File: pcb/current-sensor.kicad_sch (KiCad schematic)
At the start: 34 parts, among them U1 SS39ET, U2 TLV9064, U3 SS39ET

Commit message: Updated parts for cost
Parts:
- C1, C10, C4, C5: LCSC C106249 -> C21120; MN Yageo -> Samsung; MPN CC0603KRX7R7BB224 -> CL10B224KA8NNNC
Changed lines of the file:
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@@
 			)
 		)
-		(property "Description" "16V 220nF X7R ±10% 0603 Multilayer Ceramic Capacitors MLCC"
+		(property "Description" "25V 220nF X7R ±10% 0603 Multilayer Ceramic Capacitors MLCC"
 			(at 162.56 71.12 0)
 			(effects
@@
 			)
 		)
-		(property "MN" "Yageo"
+		(property "MN" "Samsung"
 			(at 162.56 71.12 0)
 			(effects
@@
 			)
 		)
-		(property "MPN" "CC0603KRX7R7BB224"
+		(property "MPN" "CL10B224KA8NNNC"
 			(at 162.56 71.12 0)
 			(effects
@@
 			)
 		)
-		(property "LCSC" "C106249"
+		(property "LCSC" "C21120"
 			(at 162.56 71.12 0)
 			(effects
@@
 			)
 		)
-		(property "Description" "16V 220nF X7R ±10% 0603 Multilayer Ceramic Capacitors MLCC"
+		(property "Description" "25V 220nF X7R ±10% 0603 Multilayer Ceramic Capacitors MLCC"
 			(at 194.31 77.47 0)
 			(effects
@@
 			)
 		)
-		(property "MN" "Yageo"
+		(property "MN" "Samsung"
 			(at 194.31 77.47 0)
 			(effects
@@
 			)
 		)
-		(property "MPN" "CC0603KRX7R7BB224"
+		(property "MPN" "CL10B224KA8NNNC"
 			(at 194.31 77.47 0)
 			(effects
@@
 			)
 		)
-		(property "LCSC" "C106249"
+		(property "LCSC" "C21120"
 			(at 194.31 77.47 0)
 			(effects
@@
 			)
 		)
-		(property "Description" "16V 220nF X7R ±10% 0603 Multilayer Ceramic Capacitors MLCC"
+		(property "Description" "25V 220nF X7R ±10% 0603 Multilayer Ceramic Capacitors MLCC"
 			(at 146.05 154.94 0)
 			(effects
@@
 			)
 		)
-		(property "MN" "Yageo"
+		(property "MN" "Samsung"
 			(at 146.05 154.94 0)
 			(effects
@@
 			)
 		)
-		(property "MPN" "CC0603KRX7R7BB224"
+		(property "MPN" "CL10B224KA8NNNC"
 			(at 146.05 154.94 0)
 			(effects
@@
 			)
 		)
-		(property "LCSC" "C106249"
+		(property "LCSC" "C21120"
 			(at 146.05 154.94 0)
 			(effects
@@
 			)
 		)
-		(property "Description" "16V 220nF X7R ±10% 0603 Multilayer Ceramic Capacitors MLCC"
+		(property "Description" "25V 220nF X7R ±10% 0603 Multilayer Ceramic Capacitors MLCC"
 			(at 208.28 41.91 0)
 			(effects
@@
 			)
 		)
-		(property "MN" "Yageo"
+		(property "MN" "Samsung"
 			(at 208.28 41.91 0)
 			(effects
@@
 			)
 		)
-		(property "MPN" "CC0603KRX7R7BB224"
+		(property "MPN" "CL10B224KA8NNNC"
 			(at 208.28 41.91 0)
 			(effects
@@
 			)
 		)
-		(property "LCSC" "C106249"
+		(property "LCSC" "C21120"
 			(at 208.28 41.91 0)
 			(effects

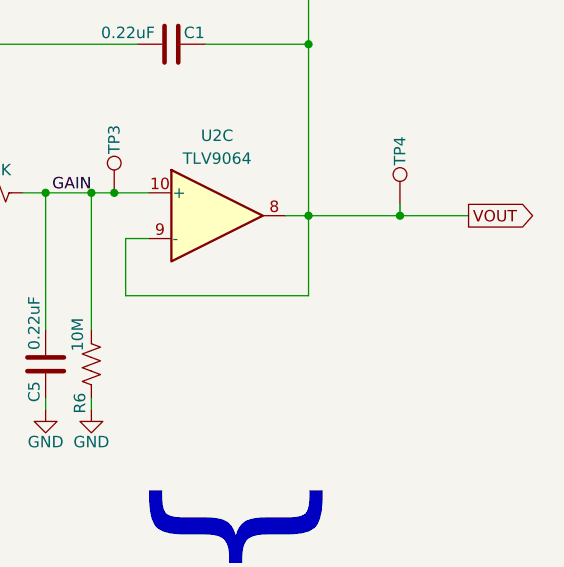
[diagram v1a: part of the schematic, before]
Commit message: Added TVS to ADC for spikes; still investigating
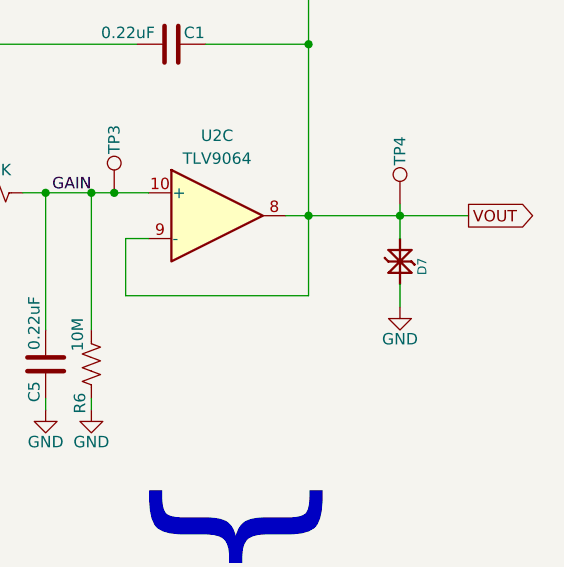
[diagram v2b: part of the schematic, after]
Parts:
- added D7: PESD3V3S1BL, CRGM Passive:DFN1006-2, symbol CRGM Passive:PESD3V3S1BL
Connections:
- net GND: now also D7.1 (K1)
- net VOUT: now also D7.2 (K2)
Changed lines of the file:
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@@
 	(wire
 		(pts
+			(xy 233.68 60.96) (xy 233.68 63.5)
+		)
+		(stroke
+			(width 0)
+			(type default)
+		)
+	)
+	(wire
+		(pts
 			(xy 123.19 74.93) (xy 123.19 55.88)
 		)
@@
 	(wire
 		(pts
+			(xy 233.68 68.58) (xy 233.68 71.12)
+		)
+		(stroke
+			(width 0)
+			(type default)
+		)
+	)
+	(wire
+		(pts
 			(xy 45.72 166.37) (xy 68.58 166.37)
 		)
@@
 	(symbol
 		(lib_id "power:GND")
+		(at 233.68 71.12 0)
+		(unit 1)
+		(exclude_from_sim no)
+		(in_bom yes)
+		(on_board yes)
+		(dnp no)
+		(property "Reference" "#PWR031"
+			(at 233.68 77.47 0)
+			(effects
+				(font
+					(size 1.27 1.27)
+				)
+				(hide yes)
+			)
+		)
+		(property "Value" "GND"
+			(at 233.68 74.676 0)
+			(effects
+				(font
+					(size 1.27 1.27)
+				)
+			)
+		)
+		(property "Footprint" ""
+			(at 233.68 71.12 0)
+			(effects
+				(font
+					(size 1.27 1.27)
+				)
+				(hide yes)
+			)
+		)
+		(property "Datasheet" ""
+			(at 233.68 71.12 0)
+			(effects
+				(font
+					(size 1.27 1.27)
+				)
+				(hide yes)
+			)
+		)
+		(property "Description" "Power symbol creates a global label with name \"GND\" , ground"
+			(at 233.68 71.12 0)
+			(effects
+				(font
+					(size 1.27 1.27)
+				)
+				(hide yes)
+			)
+		)
+		(pin "1"
+		)
+		(instances
+			(project "current-module"
+				(path "/a8149920-3b7f-4d7d-8e96-7a0b38870225/750b9b07-db7a-4289-8a61-542df9f7ebc0"
+					(reference "#PWR031")
+					(unit 1)
+				)
+			)
+		)
+	)
+	(symbol
+		(lib_id "power:GND")
 		(at 107.95 158.75 0)
 		(unit 1)
@@
 					(unit 1)
 				)
+			)
+		)
+	)
+	(symbol
+		(lib_id "CRGM Passive:PESD3V3S1BL")
+		(at 233.68 66.04 90)
+		(unit 1)
+		(exclude_from_sim no)
+		(in_bom yes)
+		(on_board yes)
+		(dnp no)
+		(property "Reference" "D7"
+			(at 236.728 67.564 0)
+			(effects
+				(font
+					(size 1 1)
+					(thickness 0.125)
+				)
+				(justify left bottom)
+			)
+		)
+		(property "Value" "PESD3V3S1BL"
+			(at 237.236 71.12 0)
+			(effects
+				(font
+					(size 1 1)
+					(thickness 0.125)
+				)
+				(justify left bottom)
+				(hide yes)
+			)
+		)
+		(property "Footprint" "CRGM Passive:DFN1006-2"
+			(at 238.76 65.786 0)
+			(effects
+				(font
+					(size 1.27 1.27)
+				)
+				(hide yes)
+			)
+		)
+		(property "Datasheet" "https://www.nexperia.com/product/PESD3V3S1BL"
+			(at 243.332 66.294 0)
+			(effects
+				(font
+					(size 1.27 1.27)
+				)
+				(hide yes)
+			)
+		)
+		(property "Description" "PESD3V3S1BL - Low capacitance bidirectional ESD protection diode\nVrwm=3.3v\nSource: https://assets.nexperia.com/documents/data-sheet/PESD3V3S1BL.pdf  Datasheet\nJLCPCB - C552521  Alternate https://jlcpcb.com/partdetail/DiodesIncorporated-DESD3V3S1BL7B/C500765 DESD3V3S1BL\nJLCPCB - C500765\nhttps://jlcpcb.com/partdetail/Fuxinsemi-LESD8D33CAT5G/C5563754 LESD8D3.3CAT5G\nJLCPCB - C5563754"
+			(at 252.73 64.516 0)
+			(effects
+				(font
+					(size 1.27 1.27)
+				)
+				(hide yes)
+			)
+		)
+		(property "LCSC" "C5563754"
+			(at 270.256 66.294 0)
+			(effects
+				(font
+					(size 1.27 1.27)
+				)
+				(hide yes)
+			)
+		)
+		(property "Digikey" "1727-PESD3V3S1BLYLTR-ND"
+			(at 268.224 65.278 0)
+			(effects
+				(font
+					(size 1.27 1.27)
+				)
+				(hide yes)
+			)
+		)
+		(property "Mouser" "621-DESD3V3S1BL-7B"
+			(at 266.192 64.516 0)
+			(effects
+				(font
+					(size 1.27 1.27)
+				)
+				(hide yes)
+			)
+		)
+		(property "MN" "FUXINSEMI"
+			(at 233.68 66.04 0)
+			(effects
+				(font
+					(size 1.27 1.27)
+				)
+				(hide yes)
+			)
+		)
+		(property "MPN" "LESD8D3.3CAT5G"
+			(at 233.68 66.04 0)
+			(effects
+				(font
+					(size 1.27 1.27)
+				)
+				(hide yes)
+			)
+		)
+		(pin "1"
+		)
+		(pin "2"
+		)
+		(instances
+			(project "current-module"
+				(path "/a8149920-3b7f-4d7d-8e96-7a0b38870225/750b9b07-db7a-4289-8a61-542df9f7ebc0"
+					(reference "D7")
+					(unit 1)
+				)

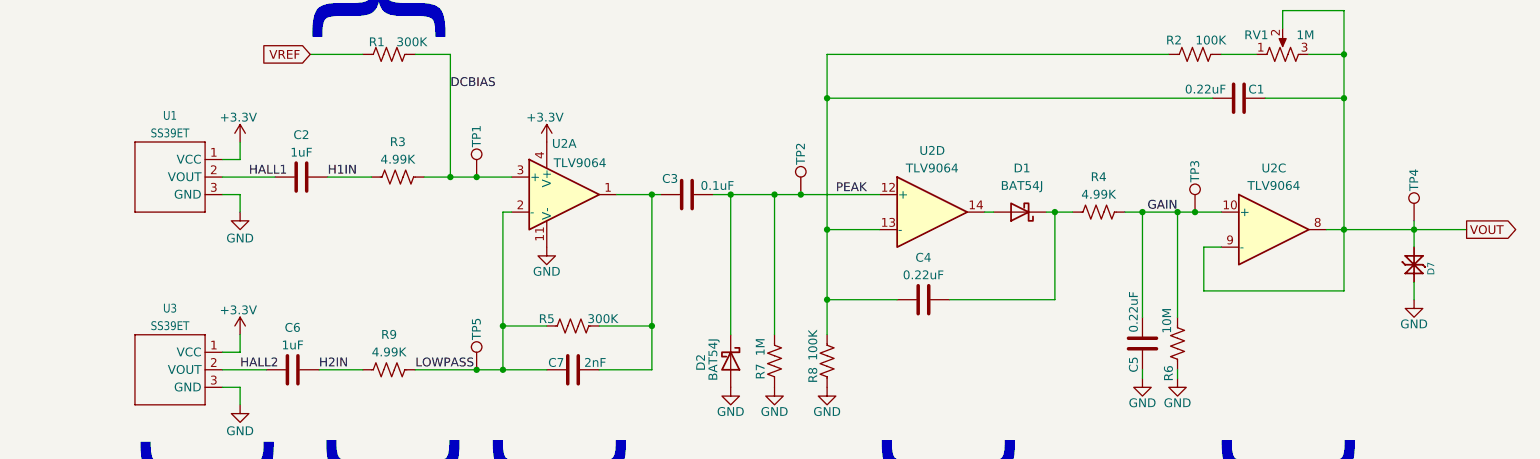
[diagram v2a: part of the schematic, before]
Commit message: Collapsed UPDI and Serial
Added indicator LEDs
Rerouted
Cleaned up silkscreen
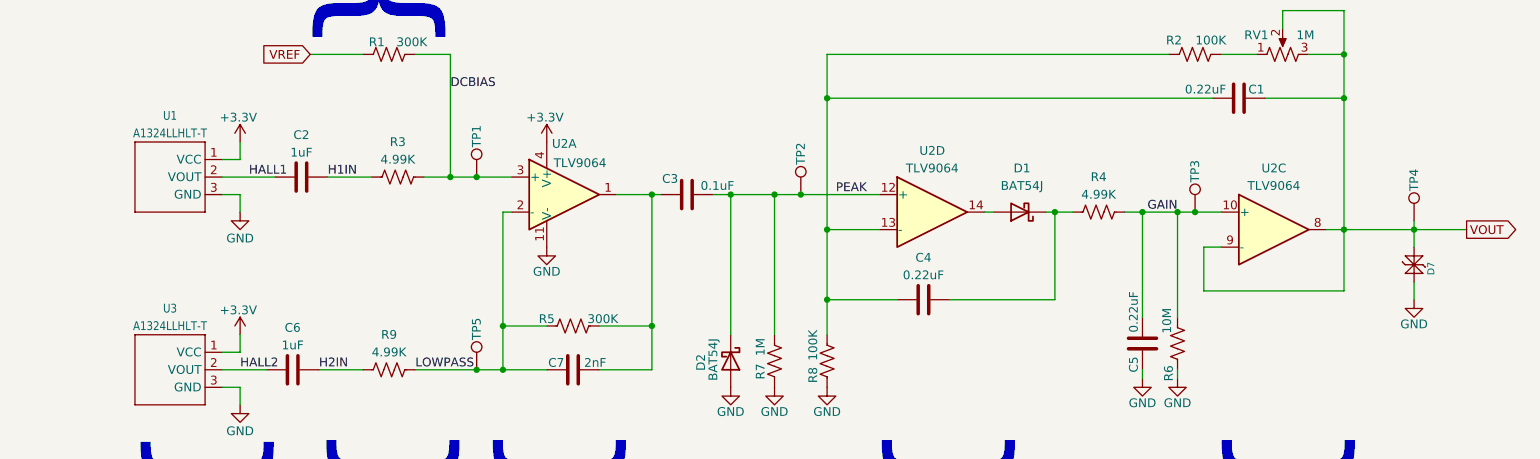
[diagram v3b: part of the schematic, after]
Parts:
- D1, D2: footprint CRGM Passive:D_SOD-323F -> Diode_SMD:D_SOD-323F
- U1: value SS39ET -> A1324LLHLT-T; footprint CRGM Passive:SOT-23 -> CRGM Passive:SOT23W; ALT (none) -> Honeywell SS39ET; Digikey 480-3845-2-ND -> 620-1402-2-ND; LCSC C126669 -> C163316; MN Honeywell -> Allegro; MPN SS39ET -> A1324LLHLT-T; Mouser 785-SS39ET -> 250-A1324LLHLX-T
- U3: value SS39ET -> A1324LLHLT-T; footprint CRGM Passive:SOT-23 -> CRGM Passive:SOT23W; ALT (none) -> ALT; Digikey 480-3845-2-ND -> 620-1402-2-ND; LCSC C126669 -> C163316; MN Honeywell -> Allegro; MPN SS39ET -> A1324LLHLT-T; Mouser 785-SS39ET -> 250-A1324LLHLX-T
